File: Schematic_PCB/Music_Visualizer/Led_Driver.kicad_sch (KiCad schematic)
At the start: 92 parts, among them U10 LM3915N-1, U11 LM3915N-1, U12 LM3915N-1, U13 LM3915N-1, U14 LM3915N-1, U15 LM3915N-1, U16 LM3915N-1, U17 NCP161ASN350T1G, U18 NCS333ASQ3T2G

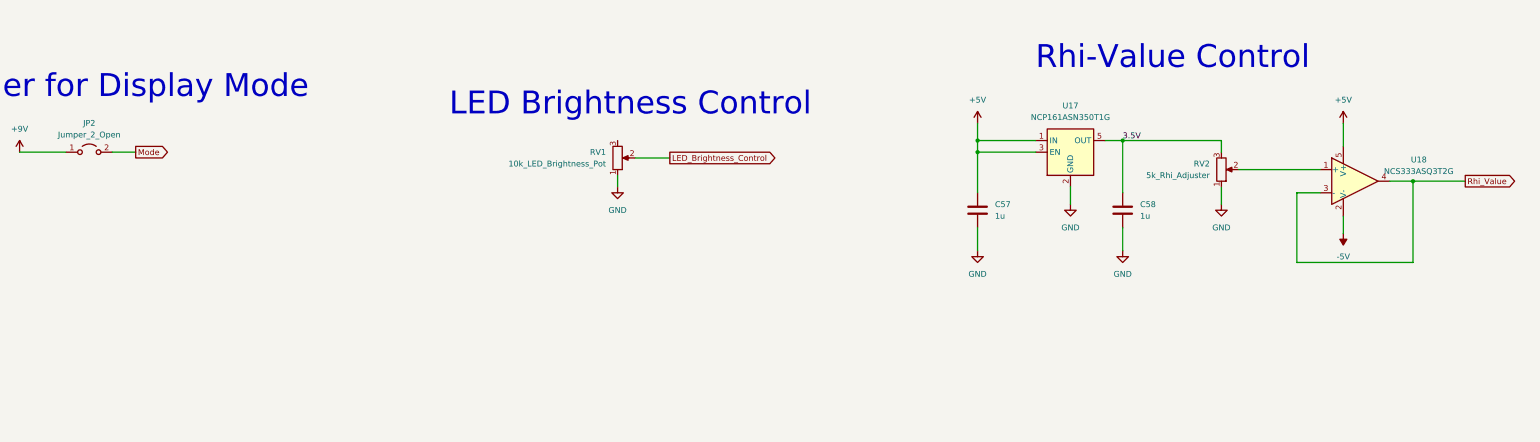
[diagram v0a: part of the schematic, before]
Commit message: RHi- Value controll replaced
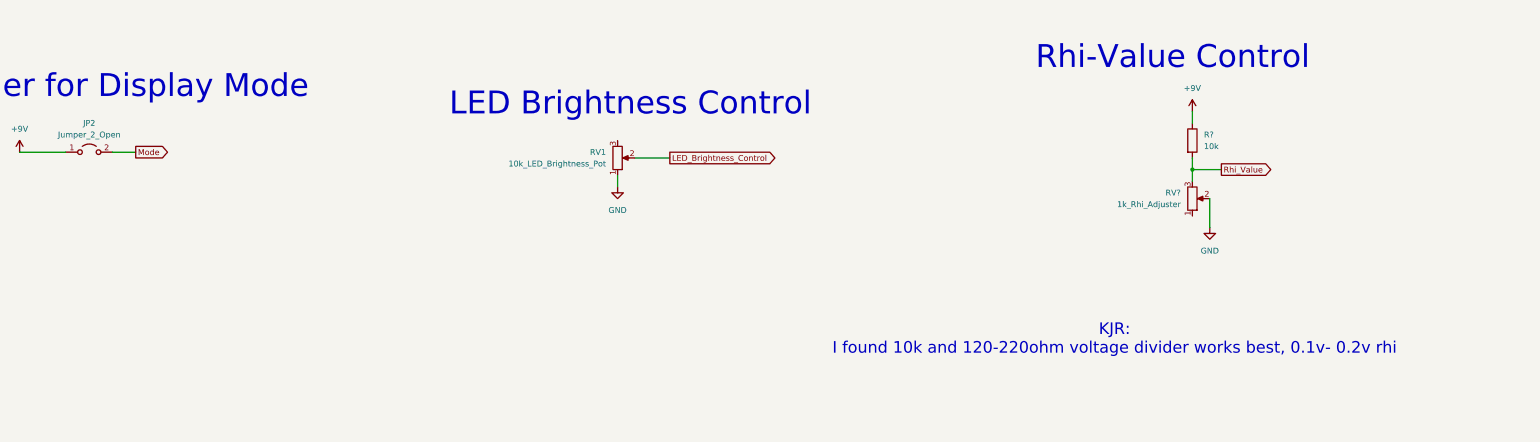
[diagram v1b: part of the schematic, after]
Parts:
- removed C57, C58: 1u, Capacitor_SMD:C_0603_1608Metric_Pad1.08x0.95mm_HandSolder, symbol Device:C
- removed U17: NCP161ASN350T1G, Package_TO_SOT_SMD:SOT-23-5, symbol Regulator_Linear:NCP718xSN120
- removed U18: NCS333ASQ3T2G, Package_TO_SOT_SMD:SOT-353_SC-70-5, symbol Amplifier_Operational:LMV321
- R?: renamed from R78; value 680 -> 10k
- RV?: renamed from RV2; value 5k_Rhi_Adjuster -> 1k_Rhi_Adjuster
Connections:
- net 3.5V is gone; now on net Rhi_Value: RV?.3
- net +9V: now also R?.1
- net GND: now also RV?.2; no longer RV?.1
- net Rhi_Value: now also R?.2
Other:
- note added: "KJR: I found 10k and 120-220ohm voltage divider works best, 0.1v- 0.2v rhi"
- moved on the sheet: RV?

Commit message: Input buffer 20-60hz filter changed
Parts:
- added R?: 10k, Resistor_SMD:R_0603_1608Metric_Pad0.98x0.95mm_HandSolder, symbol Device:R
- R78: renamed from R?; value 10k -> 680
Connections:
- net +9V: now also R?.1; no longer R78.1
- net Rhi_Value: now also R?.2; no longer R78.2
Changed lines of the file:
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@@
 		(dnp no)
 		(fields_autoplaced yes)
-		(property "Reference" "#PWR?"
+		(property "Reference" "#PWR0105"
 			(at 483.87 204.47 0)
 			(effects
@@
 			(project "Music_Visualizer"
 				(path "/236ff8a0-79ed-4eaf-ae36-90444797fa8d/56ed3a67-eed8-4688-8767-d6bf63bd87ca"
-					(reference "#PWR?")
+					(reference "#PWR0105")
 					(unit 1)
 				)

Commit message: Change freq ranges to quasi-log
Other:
- note added: "Bass: [60Hz:150Hz]"
- note added: "Low Midrange: [150Hz:400Hz]"
- note added: "Midrange: [400Hz:1kHz]"
- note added: "Presence: [2.5kHz:6kHz]"
- note added: "Upper-Midrange: [1kHz:2.5kHz]"
- note removed: "Bass: [60Hz:250Hz]"
- note removed: "Low Midrange: [250Hz:500Hz]"
- note removed: "Midrange: [500Hz:2kHz]"
- note removed: "Presence: [4kHz:6kHz]"
- note removed: "Upper-Midrange: [2kHz:4kHz]"

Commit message: Add output buffer
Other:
- note added: "Bass: [60Hz:250Hz]"
- note added: "Low Midrange: [250Hz:500Hz]"
- note added: "Midrange: [500Hz:2kHz]"
- note added: "Presence: [4kHz:6kHz]"
- note added: "Upper-Midrange: [2kHz:4kHz]"
- note removed: "Bass: [60Hz:150Hz]"
- note removed: "Low Midrange: [150Hz:400Hz]"
- note removed: "Midrange: [400Hz:1kHz]"
- note removed: "Presence: [2.5kHz:6kHz]"
- note removed: "Upper-Midrange: [1kHz:2.5kHz]"

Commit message: Change op amp exit cap
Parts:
- removed C59: 10u, Capacitor_THT:CP_Radial_D5.0mm_P2.00mm, symbol Device:C_Polarized
- D10, D11, D12, D13, D14, D15, D16, D17, D18, D19, D20, D21, D22, D23, D24, D25, D26, D27, D28, D29, D3, D30, D31, D32, D33, D34, D35, D36, D37, D38, D39, D4, D40, D41, D42, D43, D44, D45, D46, D47, D48, D49, D5, D50, D51, D52, D53, D54, D55, D56, D57, D58, D59, D6, D60, D61, D62, D63, D64, D65, D66, D67, D68, D69, D7, D70, D8, D9: footprint LED_THT:LED_D5.0mm -> LED_SMD:LED_1210_3225Metric_Pad1.42x2.65mm_HandSolder
- R75, R76, R77, R78, R79, R80, R81, R?: footprint Resistor_SMD:R_0603_1608Metric_Pad0.98x0.95mm_HandSolder -> Resistor_SMD:R_0805_2012Metric_Pad1.20x1.40mm_HandSolder

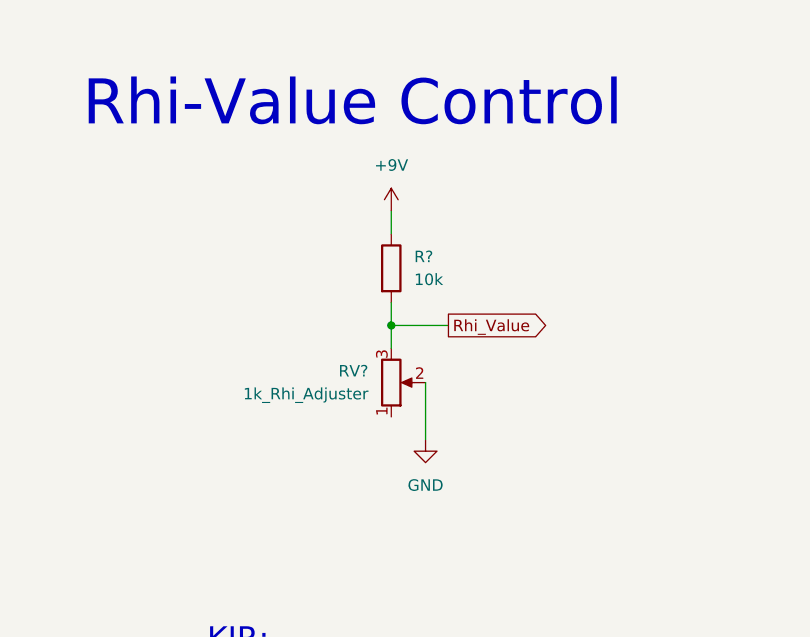
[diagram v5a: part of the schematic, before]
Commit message: Add testpoints
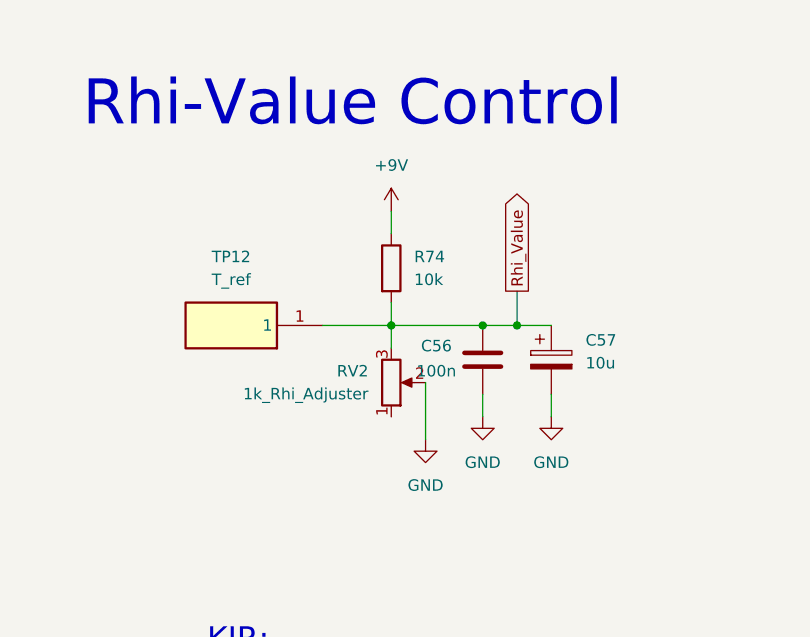
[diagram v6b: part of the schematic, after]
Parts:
- added C56: 100n, Capacitor_SMD:C_0805_2012Metric_Pad1.18x1.45mm_HandSolder, symbol Device:C
- added C57: 10u, Capacitor_THT:CP_Radial_D5.0mm_P2.00mm, symbol Device:C_Polarized
- added TP12: T_ref, Custom_Footprints:TEST1Y, symbol TEST-1_Y_:TEST-1_Y_
- gave numbers to parts that had none: 2
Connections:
- net GND: now also C56.1, C57.2
- net Rhi_Value: now also C56.2, C57.1, TP12.1

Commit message: In-Out switch
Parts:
- D1, D2: footprint LED_THT:LED_D5.0mm -> LED_SMD:LED_1210_3225Metric_Pad1.42x2.65mm_HandSolder
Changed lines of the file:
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@@
 			)
 		)
-		(property "Footprint" "LED_THT:LED_D5.0mm"
+		(property "Footprint" "LED_SMD:LED_1210_3225Metric_Pad1.42x2.65mm_HandSolder"
 			(at 62.23 54.61 0)
 			(effects
@@
 			)
 		)
-		(property "Footprint" "LED_THT:LED_D5.0mm"
+		(property "Footprint" "LED_SMD:LED_1210_3225Metric_Pad1.42x2.65mm_HandSolder"
 			(at 52.07 54.61 0)
 			(effects

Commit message: PCB V1 done
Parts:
- C56: footprint Capacitor_SMD:C_0805_2012Metric_Pad1.18x1.45mm_HandSolder -> Custom_Footprints:C_0805_2012Metric_Pad1.18x1.45mm_HandSolder
- R74, R75, R76, R77, R78, R79, R80, R81: footprint Resistor_SMD:R_0805_2012Metric_Pad1.20x1.40mm_HandSolder -> Custom_Footprints:R_0805_2012Metric_Pad1.20x1.40mm_HandSolder
- RV1: value 10k_LED_Brightness_Pot -> 1k_LED_Brightness_Pot; footprint PTV09A_Pot_Vertical:PTV09 -> Potentiometer_THT:Potentiometer_Runtron_RM-065_Vertical
- RV2: footprint PTV09A_Pot_Vertical:PTV09 -> Potentiometer_THT:Potentiometer_Runtron_RM-065_Vertical
